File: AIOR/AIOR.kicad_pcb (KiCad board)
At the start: 2 copper layers, 85 x 56.5 mm, 157 parts, among them J20 Conn_01x04, J30 Conn_01x02, J31 Conn_01x02, J50 Conn_01x02, J70 Conn_01x01, J81 Conn_01x06, J82 5V 12V, J90 Conn_01x03, P1 CONN_02X20, P2 CONN_01X02, P3 CAN, P50 XPN, P60 SLX, P70 LCN, P8 Conn_01x02, P9 Conn_01x04, Q30 BTN8982TA, Q31 BTN8982TA, Q60 BC817, Q70 BC817, Q90 BC857, Q91 BC857, U1 MCP2517FD, U2 ISO1050, U20 L7833, U21 L7805, U22 DSPIC33EP128GM604, U23 Si8605, U24 MCP2562, U4 P82B715, U40 C8051F502, U41 ADUM1251, U42 MCP2561, U50 MAX3072E, U70 LM393, U81 L7805, U82 SI8641-SOIC, U83 4504, U90 SAA6579, Y1 4MHz, Y20 8MHz, Y90 4MHz

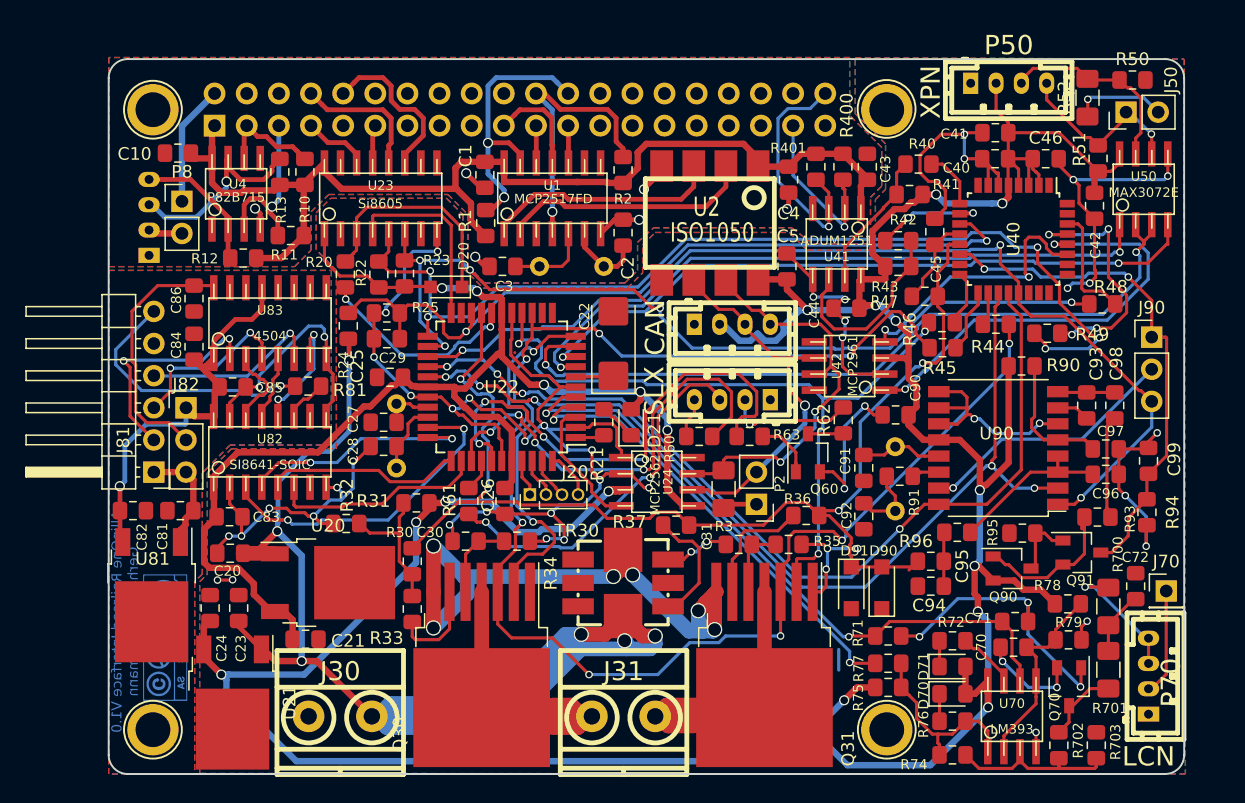
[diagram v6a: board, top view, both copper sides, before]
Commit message: dsPIC PIN assignement fixed and opimized
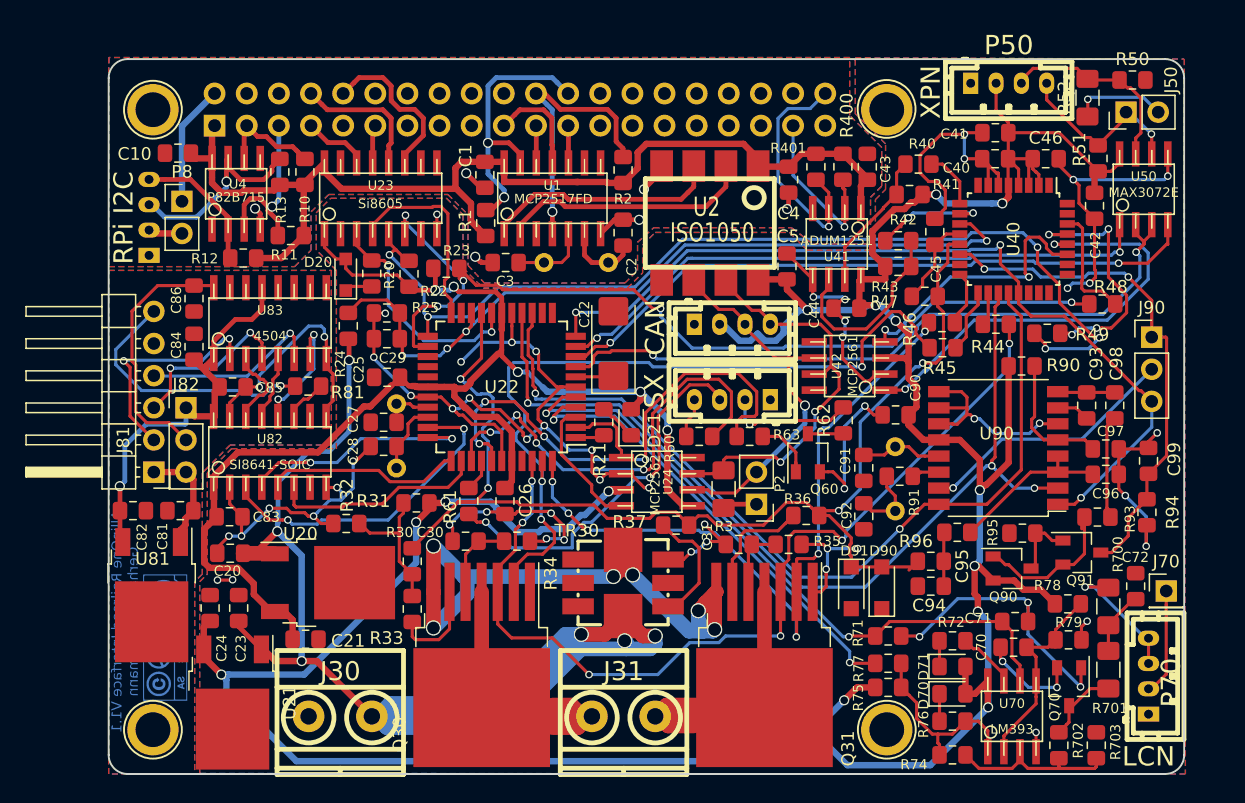
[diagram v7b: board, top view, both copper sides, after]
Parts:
- removed J20: Conn_01x04, Connector_PinHeader_1.27mm:PinHeader_1x04_P1.27mm_Vertical
- J81: value Conn_01x06 -> S88
- P60: value SLX -> SX
- R22, R23: value 3k3 -> 1k
- R24: value 18k -> 22k
- RPi I2C: renamed from P9
- moved D20 8.01 mm to (146.7, 88.5), turned to 90 degrees
- moved R23 3.33 mm to (154.7, 88.0), turned to 0 degrees
- moved R22 2.39 mm to (151.7, 88.5)
- moved R20 2.08 mm to (148.8, 88.4), turned to 270 degrees
- moved Y1 0.47 mm to (164.9, 87.6)
- moved C3 0.40 mm to (159.4, 87.6)
- moved C25 0.24 mm to (150.0, 96.6)
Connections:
- D20 pad 1: /MCLR -> Net-(D20-Pad1)
- R20 pad 1: Net-(R20-Pad1) -> /MCLR
- R20 pad 2: /MCLR -> Net-(D20-Pad1)
- U22 pad 10: /RS485_EN -> /RS485_RX
- U22 pad 11: /B_ENA -> /QUAL
- U22 pad 14: /B_LEFT -> /RDCL
- U22 pad 15: /B_RIGHT -> /RDDA
- U22 pad 18: Net-(R20-Pad1) -> /MCLR
- U22 pad 25: /QUAL -> Net-(U22-Pad25)
- U22 pad 26: /RDCL -> Net-(U22-Pad26)
- U22 pad 27: /RDDA -> Net-(U22-Pad27)
- U22 pad 42: /RB6 -> /B_ENA
- U22 pad 43: /RB7 -> /B_LEFT
- U22 pad 44: /RB8 -> /B_RIGHT
- U22 pad 8: /RS485_RX -> /RS485_EN
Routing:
- net Net-(R20-Pad1): track 16.4 -> 0.00 mm, vias 2 -> 0
- net /B_ENA: track 90.4 -> 74.6 mm
- net /QUAL: track 79.9 -> 68.6 mm
- net GNDA: track 240.7 -> 232.4 mm, vias 50 -> 54
- net /RS485_EN: track 61.3 -> 54.9 mm
- net /RS485_RX: track 52.7 -> 48.4 mm
- net /RB8: track 3.81 -> 0.00 mm
- net /RB7: track 3.31 -> 0.00 mm
- net /RB6: track 3.22 -> 0.00 mm
- net /PGD: track 70.2 -> 73.3 mm
- net /RDCL: track 72.3 -> 69.3 mm, vias 4 -> 2
- net /RB5: track 2.92 -> 0.00 mm
- net Net-(D20-Pad1): track 0.00 -> 2.19 mm
- net /RS485_TX: track 54.2 -> 52.2 mm
- net /RDDA: track 75.8 -> 73.8 mm, vias 5 -> 3
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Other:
- board text added: "AllinOne Railroad Interface V1.1 Gerhard Bertelsmann"
- board text removed: "AllinOne Railroad Interface V1.0 Gerhard Bertelsmann"

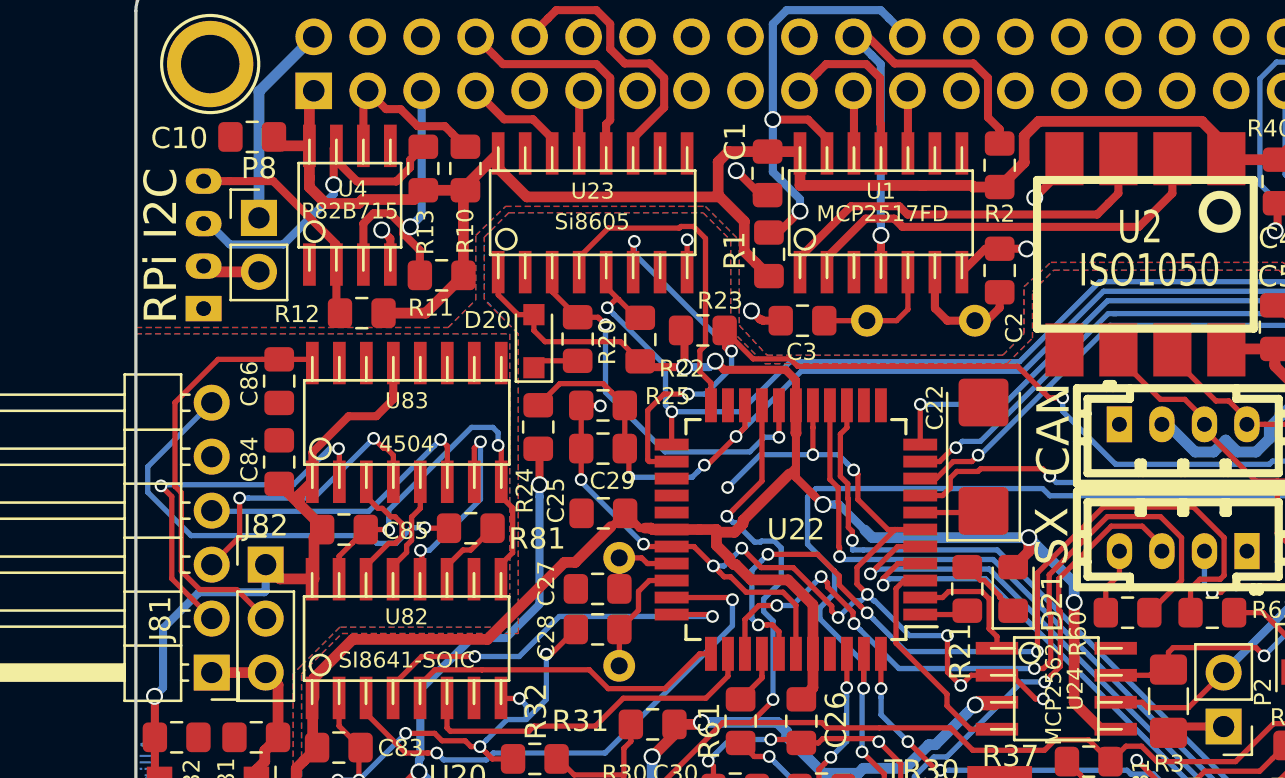
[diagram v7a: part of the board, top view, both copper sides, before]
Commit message: fix CAN transceiver STDBY
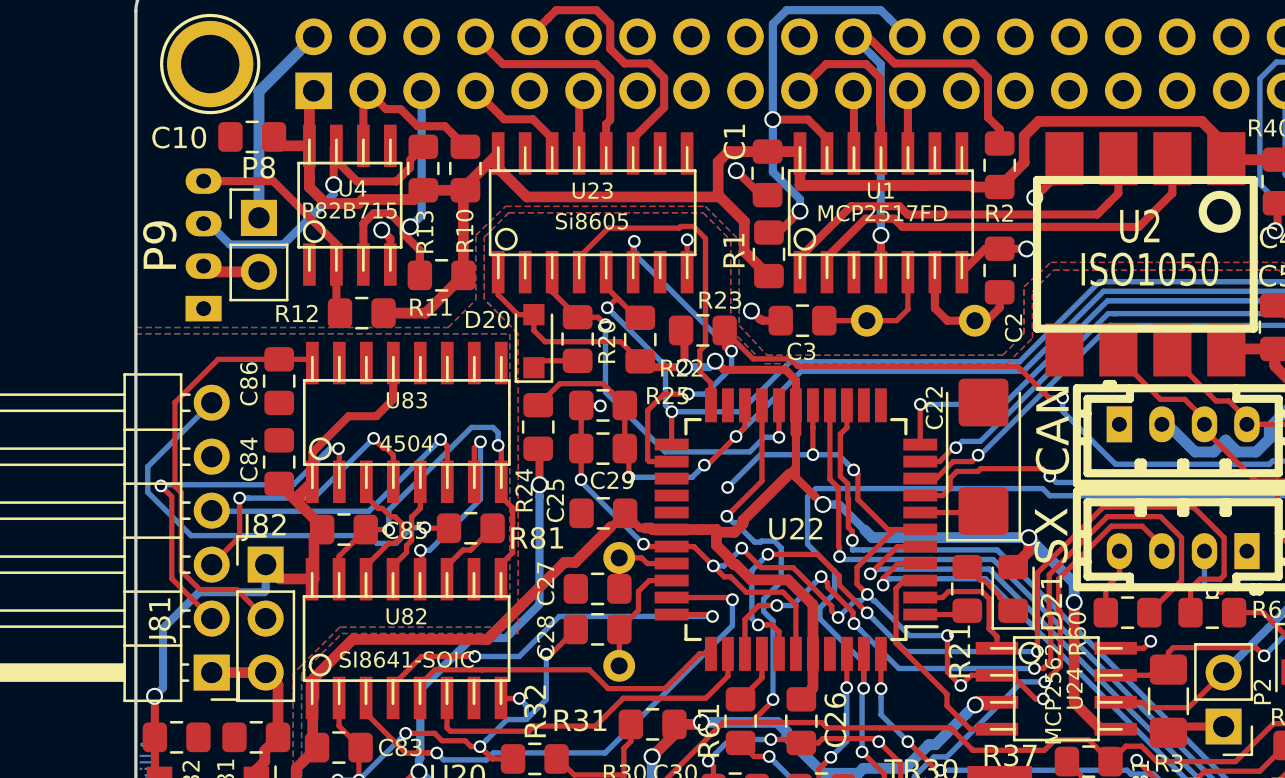
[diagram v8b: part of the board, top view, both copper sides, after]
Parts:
- J81: value S88 -> Conn_01x06
- P9: renamed from RPi I2C
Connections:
- U24 pad 8: Net-(U24-Pad8) -> GNDA
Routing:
- net GNDA: track 232.4 -> 234.2 mm, vias 54 -> 55
